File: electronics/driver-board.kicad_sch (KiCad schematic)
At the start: 67 parts, among them J1 Conn_01x02, J3 Motor_Conn_01x04, J5 Conn_01x06_Female, SW1 SW_Push, SW2 SW_Push, U2 LMR16020PDDAR, U3 ESP32-C6-MINI-1/U, U4 AMS1117-3.3, U5 TMC5240-TSSOP38, U6 MT6835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

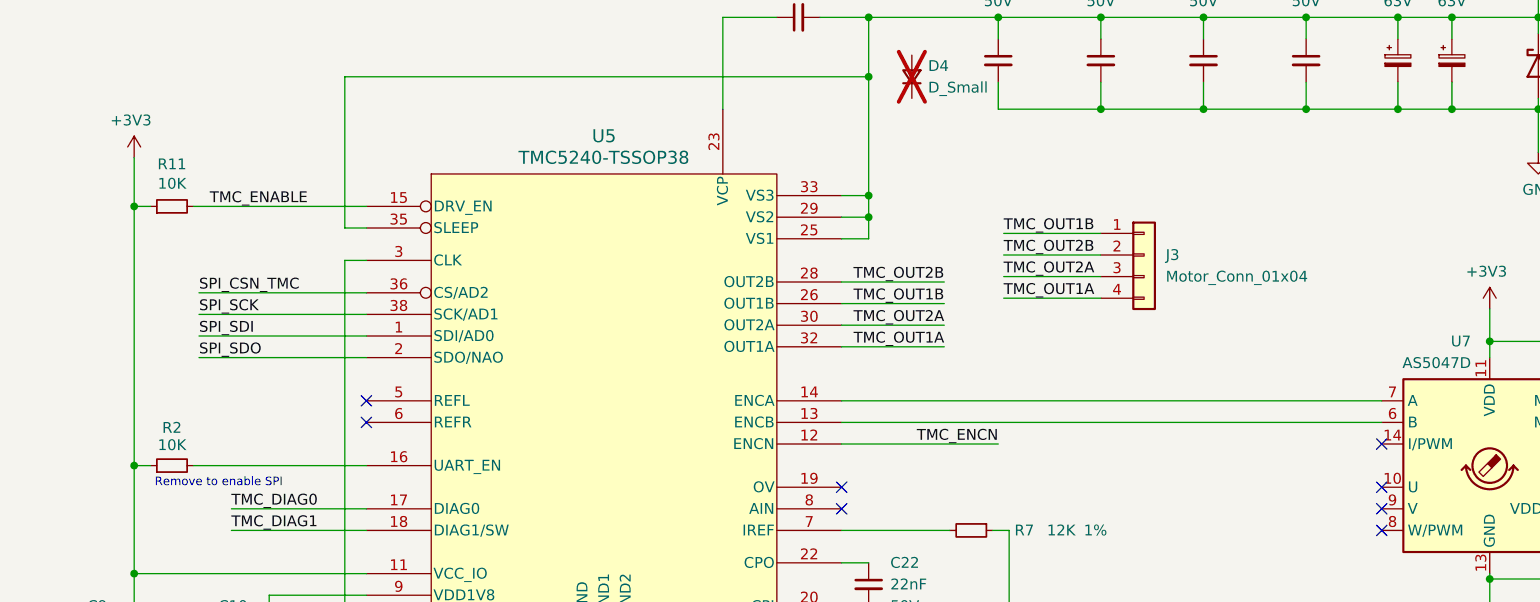
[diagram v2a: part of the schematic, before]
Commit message: connected encoder index
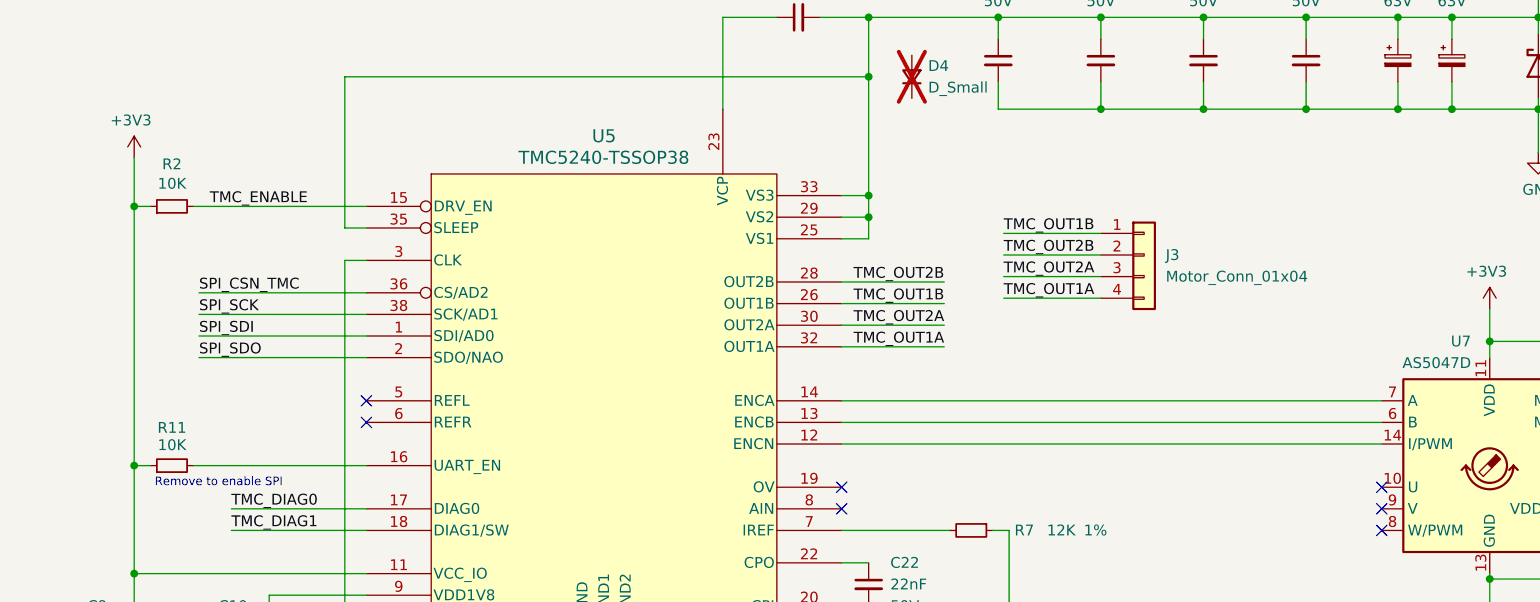
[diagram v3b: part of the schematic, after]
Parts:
- renumbered R2 to R11, R11 to R2
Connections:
- net TMC_ENCN is gone; now on an unnamed net: U5.12 (ENCN)
- no-connect marks 16 -> 15
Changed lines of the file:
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@@
   (no_connect (at 182.88 161.925))
   (no_connect (at 361.315 201.295))
-  (no_connect (at 182.88 156.845))
   (no_connect (at 335.915 196.85))
   (no_connect (at 335.915 191.77))
@@
     (stroke (width 0) (type default))
   )
-  (wire (pts (xy 119.38 156.845) (xy 137.795 156.845))
-    (stroke (width 0) (type default))
-  )
   (wire (pts (xy 96.52 57.785) (xy 96.52 60.325))
     (stroke (width 0) (type default))
@@
     (stroke (width 0) (type default))
   )
+  (wire (pts (xy 119.38 156.845) (xy 182.88 156.845))
+    (stroke (width 0) (type default))
+  )
   (wire (pts (xy 195.58 172.72) (xy 195.58 172.085))
     (stroke (width 0) (type default))
@@
     (effects (font (size 1 1)) (justify right bottom))
   )
-  (label "TMC_ENCN" (at 137.795 156.845 180) (fields_autoplaced)
-    (effects (font (size 1.27 1.27)) (justify right bottom))
-  )
   (label "ESP_UART_RXD" (at 380.365 43.815 180) (fields_autoplaced)
     (effects (font (size 1.27 1.27)) (justify right bottom))
@@
   (symbol (lib_id "Device:R_Small") (at 40.64 159.385 90) (unit 1)
     (in_bom yes) (on_board yes) (dnp no)
-    (property "Reference" "R2" (at 40.64 154.94 90)
+    (property "Reference" "R11" (at 40.64 154.94 90)
       (effects (font (size 1.27 1.27)))
     )
@@
       (project "driver-board"
         (path "/597a11f2-5d2c-4a65-ac95-38ad106e1367"
-          (reference "R2") (unit 1)
+          (reference "R11") (unit 1)
         )
       )
@@
   (symbol (lib_id "Device:R_Small") (at 40.64 128.905 90) (unit 1)
     (in_bom yes) (on_board yes) (dnp no)
-    (property "Reference" "R11" (at 40.64 123.952 90)
+    (property "Reference" "R2" (at 40.64 123.952 90)
       (effects (font (size 1.27 1.27)))
     )
@@
       (project "driver-board"
         (path "/597a11f2-5d2c-4a65-ac95-38ad106e1367"
-          (reference "R11") (unit 1)
+          (reference "R2") (unit 1)
         )
       )

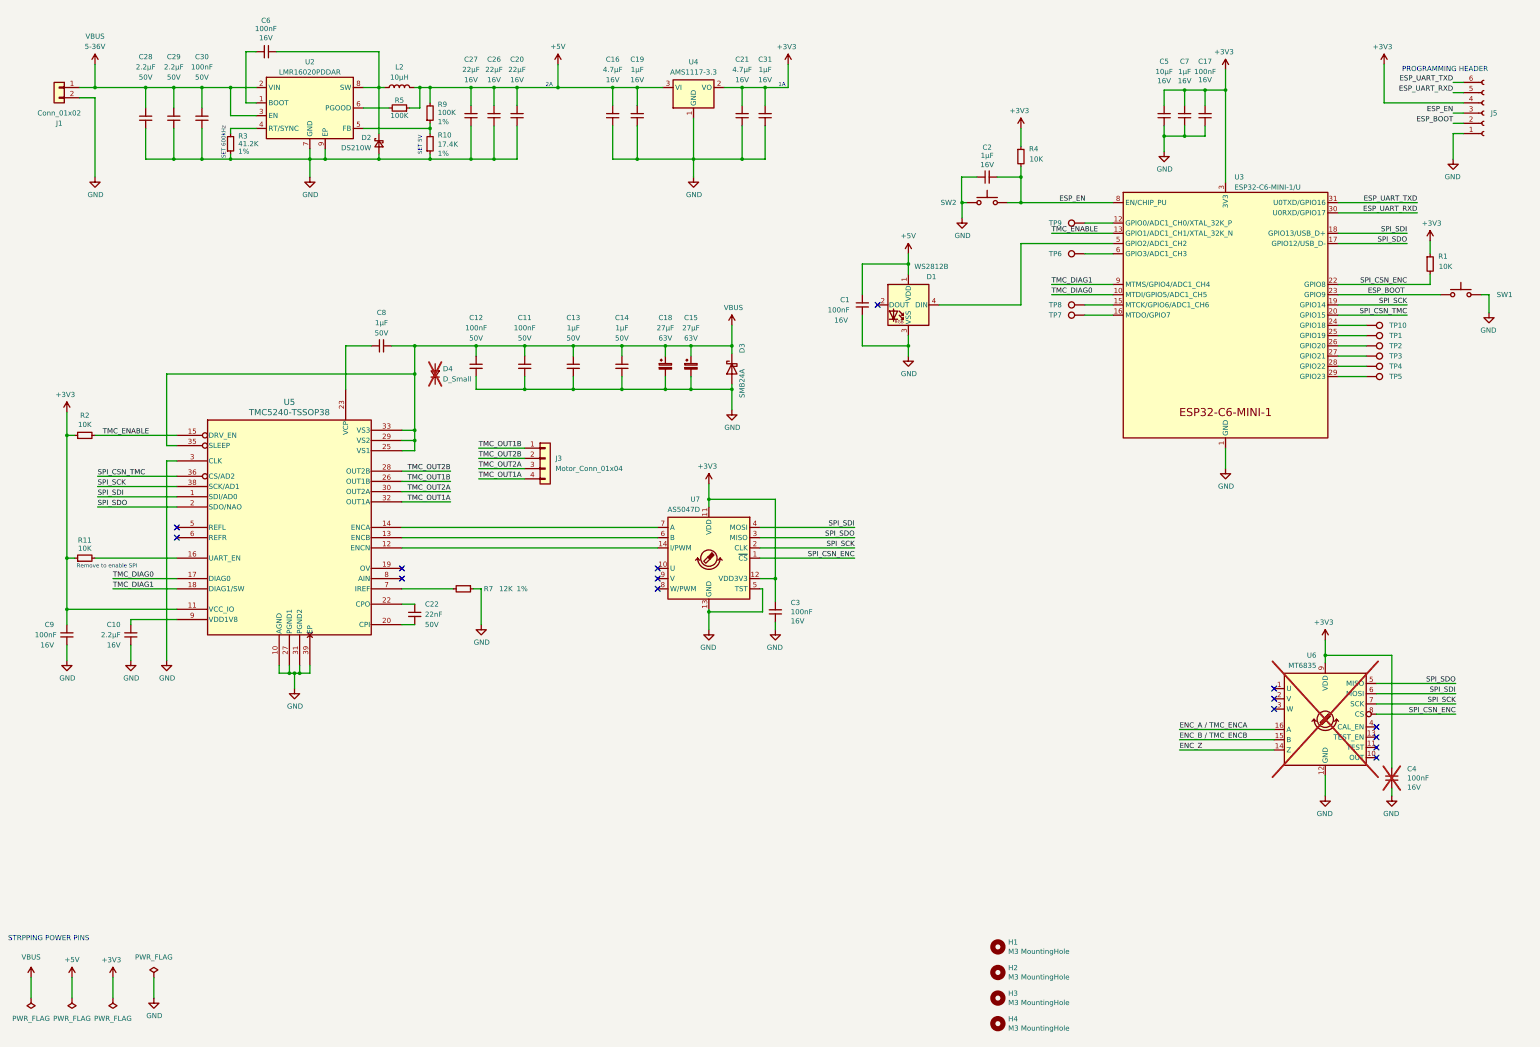
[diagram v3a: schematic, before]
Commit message: new board layout; stripped 5v line and added qwiic and some buttons
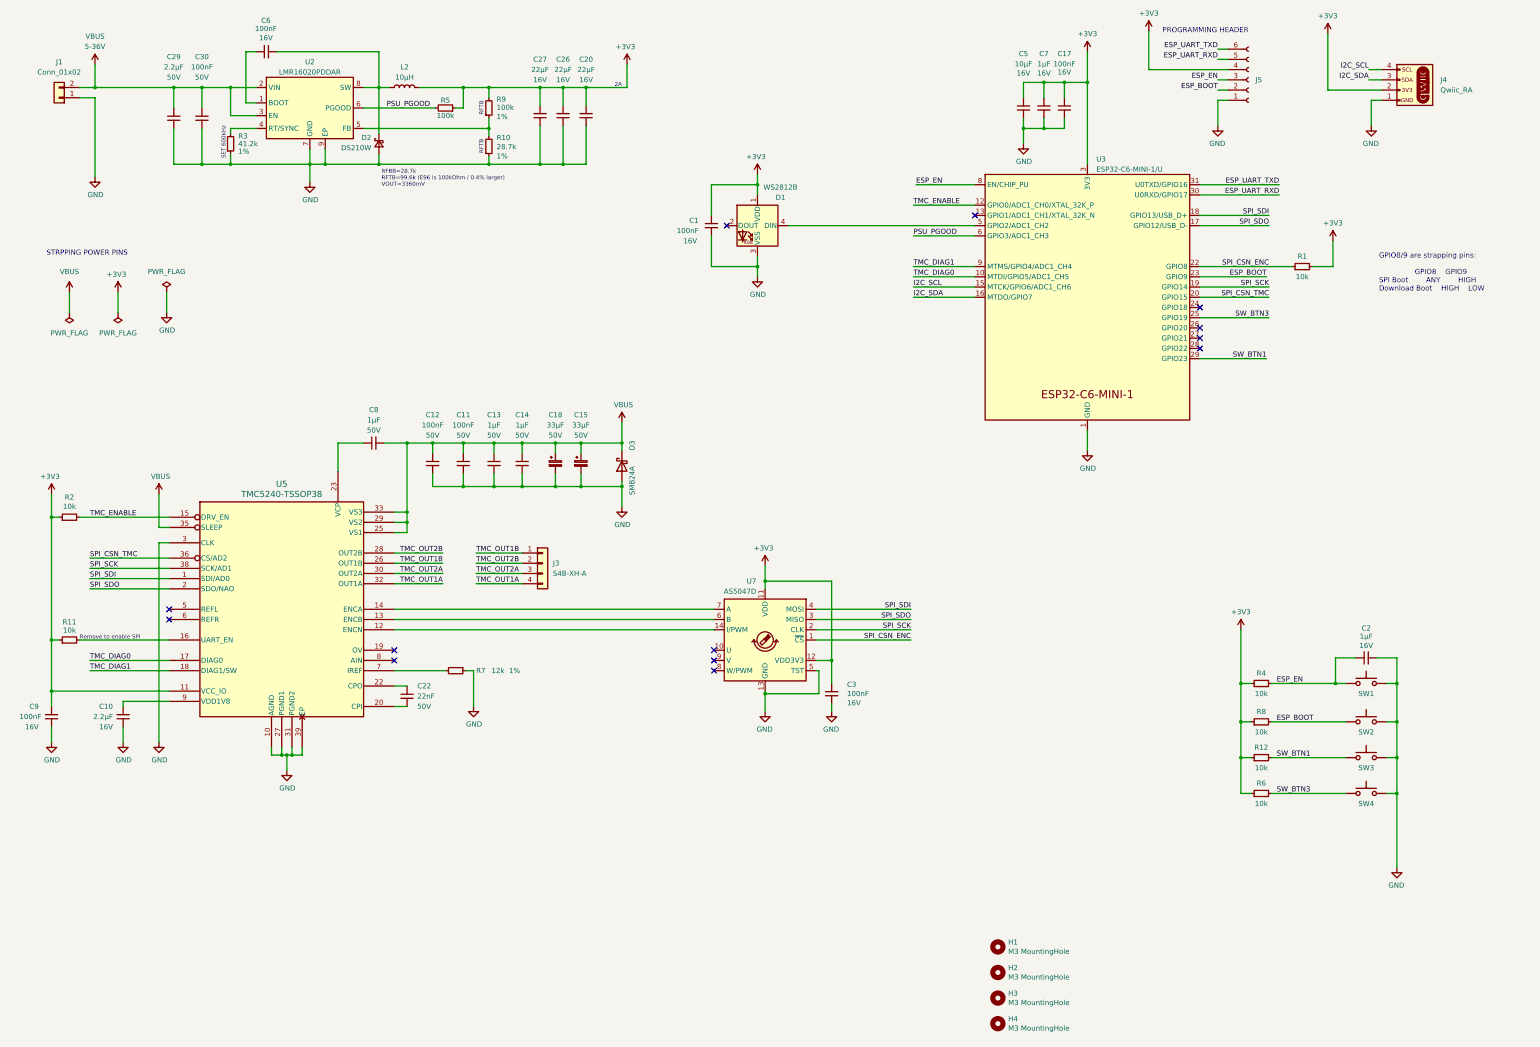
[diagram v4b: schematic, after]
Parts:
- removed C16, C21: 4.7µF, Capacitor_SMD:C_0603_1608Metric, symbol Device:C_Small
- removed C19, C31: 1µF, Capacitor_SMD:C_0603_1608Metric, symbol Device:C_Small
- removed C28: 2.2µF, Capacitor_SMD:C_0603_1608Metric, symbol Device:C_Small
- removed C4: 100nF, Capacitor_SMD:C_0603_1608Metric, symbol Device:C_Small
- removed D4: D_Small, symbol Device:D_Small
- removed TP1, TP10, TP2, TP3, TP4, TP5, TP6, TP7, TP8, TP9: TestPoint, TestPoint:TestPoint_Pad_D1.0mm, symbol Connector:TestPoint
- removed U4: AMS1117-3.3, Package_TO_SOT_SMD:SOT-223-3_TabPin2, symbol Regulator_Linear:AMS1117-3.3
- removed U6: MT6835, Package_SO:TSSOP-16_4.4x5mm_P0.65mm, symbol Slimc_Sensor_Magnetic:MT6835
- added J4: Qwiic_RA, SparkFun-Connector:JST04_1MM_RA, symbol SparkFun-Connector:Qwiic_Right_Angle
- added R12, R6, R8: 10k, Resistor_SMD:R_0603_1608Metric, symbol Device:R_Small
- added SW2, SW4: SW_Push, Slimc_Button_Switch_SMD:SW_Push_1P1T_TS-1145-X-B, symbol Switch:SW_Push
- C15, C18: value 27µF -> 33µF; LCSC C487378 -> C487356; Manf# VKMB1001J270MV -> VKMB1001H330MV; Voltage 63V -> 50V
- J1: footprint Slimc_Connector_Wago:2060-472&slash_998-404 -> Connector_JST:JST_XH_B2B-XH-A_1x02_P2.50mm_Vertical
- J3: value Motor_Conn_01x04 -> S4B-XH-A
- R1, R11, R2, R4: value 10K -> 10k
- R10: value 17.4K -> 28.7k; LCSC C863611 -> C245945; Manf# RT0603FRE0717K4L -> RC0603FR-0728K7L
- R3: value 41.2K -> 41.2k
- R5, R9: value 100K -> 100k
- R7: value 12K -> 12k
- SW3: renamed from SW1; footprint Button_Switch_SMD:SW_SPST_B3U-1000P -> Slimc_Button_Switch_SMD:SW_Push_1P1T_TS-1145-X-B; LCSC C231329 -> C5146819; Manf Omron Electronics -> XKB Connectivity; Manf# B3U-1000P -> TS-1145-B-B
- renumbered SW2 to SW1
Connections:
- net +5V is gone; now on net +3V3: C1.1, C20.2, C26.2, C27.2, D1.1 (VDD), L2.2, R5.1, R9.2
- net +3V3: now also R1.2, J4.2 (Pin_2), R12.1, R6.1, R8.1; no longer R1.1
- net ESP_BOOT: now also R8.2, SW2.2; no longer SW3.2
- net ESP_EN: now also C2.1, SW1.1; no longer C2.2, SW1.2
- net GND: now also C2.2, J1.1 (Pin_1), SW1.2, J4.1 (Pin_1), SW2.1, SW4.1; no longer C2.1, J1.2 (Pin_2), SW1.1
- net SPI_CSN_ENC: now also R1.1; no longer R1.2
- net TMC_ENABLE: now also U3.12 (GPIO0/ADC1_CH0/XTAL_32K_P); no longer U3.13 (GPIO1/ADC1_CH1/XTAL_32K_N)
- net VBUS: now also J1.2 (Pin_2); no longer J1.1 (Pin_1)
- net PSU_PGOOD: now reaches R5.2, U2.6 (PGOOD)
- net PSU_PGOOD: now also U3.6 (GPIO3/ADC1_CH3)
- net SW_BTN1: now reaches U3.29 (GPIO23)
- net SW_BTN1: now also SW3.2, R12.2
- net SW_BTN3: now reaches U3.25 (GPIO19)
- net SW_BTN3: now also R6.2, SW4.2
- net I2C_SCL: now reaches U3.15 (MTCK/GPIO6/ADC1_CH6)
- net I2C_SCL: now also J4.4 (Pin_4)
- net I2C_SDA: now reaches U3.16 (MTDO/GPIO7)
- net I2C_SDA: now also J4.3 (Pin_3)
- new net: J4.NC1 (NC), J4.NC2 (NC)
- no-connect marks 15 -> 13
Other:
- note added: "GPIO8/9 are strapping pins: GPIO8 GPIO9 SPI Boot ANY HIGH Download Boot HIGH LOW"
- note added: "RFBB=28.7k RFTB=99.6k (E96 is 100kOhm / 0.4% larger) VOUT=3360mV"
- note added: "RFTB"
- note removed: "1A"
- note removed: "SET 5V"
- moved on the sheet: C1, C10, C11, C12, C13, C14, C17, C18, C2, C20, C22, C26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

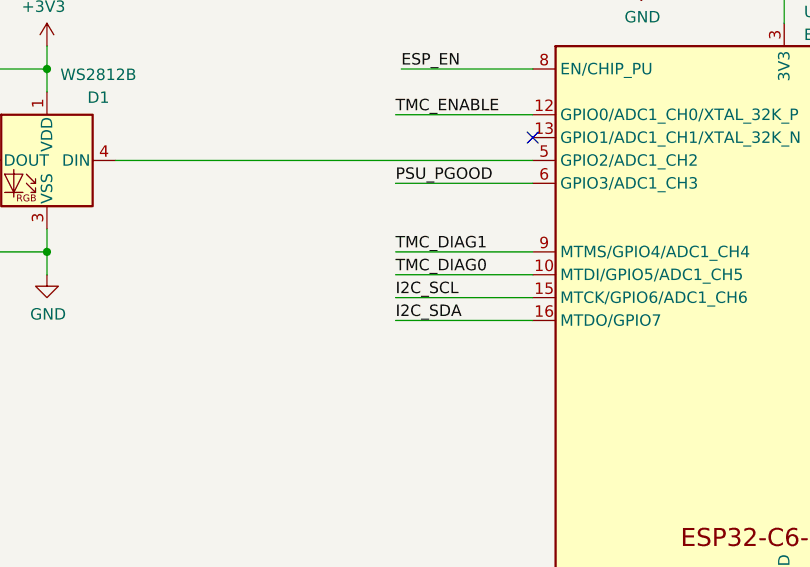
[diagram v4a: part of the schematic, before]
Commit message: pull ups for i2c; teardrops on through hole connections
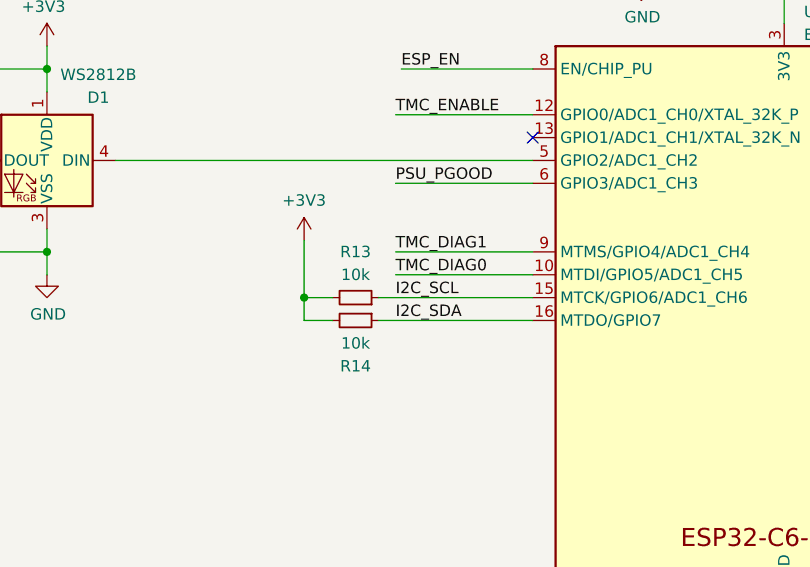
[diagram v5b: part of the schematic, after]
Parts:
- added R13, R14: 10k, Resistor_SMD:R_0603_1608Metric, symbol Device:R_Small
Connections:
- net +3V3: now also R13.2, R14.2
- net I2C_SCL: now also R13.1
- net I2C_SDA: now also R14.1
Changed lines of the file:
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@@
   (junction (at 289.56 41.275) (diameter 0) (color 0 0 0 0)
   )
+  (junction (at 236.22 92.075) (diameter 0) (color 0 0 0 0)
+  )
   (junction (at 120.65 147.955) (diameter 0) (color 0 0 0 0)
   )
@@
     (stroke (width 0) (type default))
   )
-  (wire (pts (xy 261.62 94.615) (xy 246.38 94.615))
+  (wire (pts (xy 261.62 94.615) (xy 244.475 94.615))
     (stroke (width 0) (type default))
   )
@@
     (stroke (width 0) (type default))
   )
+  (wire (pts (xy 236.22 94.615) (xy 236.22 92.075))
+    (stroke (width 0) (type default))
+  )
   (wire (pts (xy 222.885 187.325) (xy 222.885 193.04))
     (stroke (width 0) (type default))
@@
     (stroke (width 0) (type default))
   )
+  (wire (pts (xy 236.22 85.725) (xy 236.22 92.075))
+    (stroke (width 0) (type default))
+  )
   (wire (pts (xy 351.155 190.5) (xy 353.695 190.5))
     (stroke (width 0) (type default))
@@
     (stroke (width 0) (type default))
   )
-  (wire (pts (xy 261.62 92.075) (xy 246.38 92.075))
+  (wire (pts (xy 261.62 92.075) (xy 244.475 92.075))
     (stroke (width 0) (type default))
   )
@@
     (stroke (width 0) (type default))
   )
+  (wire (pts (xy 239.395 92.075) (xy 236.22 92.075))
+    (stroke (width 0) (type default))
+  )
   (wire (pts (xy 278.765 45.085) (xy 278.765 41.275))
     (stroke (width 0) (type default))
@@
     (stroke (width 0) (type default))
   )
+  (wire (pts (xy 239.395 94.615) (xy 236.22 94.615))
+    (stroke (width 0) (type default))
+  )
   (wire (pts (xy 245.745 172.085) (xy 222.25 172.085))
     (stroke (width 0) (type default))
@@
     )
   )
+  (symbol (lib_id "Device:R_Small") (at 241.935 94.615 270) (unit 1)
+    (in_bom yes) (on_board yes) (dnp no)
+    (property "Reference" "R14" (at 241.935 99.695 90)
+      (effects (font (size 1.27 1.27)))
+    )
+    (property "Value" "10k" (at 241.935 97.155 90)
+      (effects (font (size 1.27 1.27)))
+    )
+    (property "Footprint" "Resistor_SMD:R_0603_1608Metric" (at 241.935 94.615 0)
+      (effects (font (size 1.27 1.27)) hide)
+    )
+    (property "Datasheet" "~" (at 241.935 94.615 0)
+      (effects (font (size 1.27 1.27)) hide)
+    )
+    (property "Manf#" "RT0603FRE1310KL" (at 241.935 94.615 0)
+      (effects (font (size 1.27 1.27)) hide)
+    )
+    (property "LCSC" "C4226066" (at 241.935 94.615 0)
+      (effects (font (size 1.27 1.27)) hide)
+    )
+    (property "Package" "0603" (at 241.935 94.615 0)
+      (effects (font (size 1.27 1.27)) hide)
+    )
+    (pin "1")
+    (pin "2")
+    (instances
+      (project "driver-board"
+        (path "/597a11f2-5d2c-4a65-ac95-38ad106e1367"
+          (reference "R14") (unit 1)
+        )
+      )
+    )
+  )
   (symbol (lib_id "Device:C_Small") (at 50.165 198.755 180) (unit 1)
     (in_bom yes) (on_board yes) (dnp no)
@@
     )
   )
+  (symbol (lib_id "Device:R_Small") (at 241.935 92.075 270) (mirror x) (unit 1)
+    (in_bom yes) (on_board yes) (dnp no)
+    (property "Reference" "R13" (at 241.935 86.995 90)
+      (effects (font (size 1.27 1.27)))
+    )
+    (property "Value" "10k" (at 241.935 89.535 90)
+      (effects (font (size 1.27 1.27)))
+    )
+    (property "Footprint" "Resistor_SMD:R_0603_1608Metric" (at 241.935 92.075 0)
+      (effects (font (size 1.27 1.27)) hide)
+    )
+    (property "Datasheet" "~" (at 241.935 92.075 0)
+      (effects (font (size 1.27 1.27)) hide)
+    )
+    (property "Manf#" "RT0603FRE1310KL" (at 241.935 92.075 0)
+      (effects (font (size 1.27 1.27)) hide)
+    )
+    (property "LCSC" "C4226066" (at 241.935 92.075 0)
+      (effects (font (size 1.27 1.27)) hide)
+    )
+    (property "Package" "0603" (at 241.935 92.075 0)
+      (effects (font (size 1.27 1.27)) hide)
+    )
+    (pin "1")
+    (pin "2")
+    (instances
+      (project "driver-board"
+        (path "/597a11f2-5d2c-4a65-ac95-38ad106e1367"
+          (reference "R13") (unit 1)
+        )
+      )
+    )
+  )
   (symbol (lib_id "Device:R_Small") (at 36.83 149.225 90) (unit 1)
     (in_bom yes) (on_board yes) (dnp no)
@@
         )
       )
+    )
+  )
+  (symbol (lib_id "power:+3V3") (at 236.22 85.725 0) (mirror y) (unit 1)
+    (in_bom yes) (on_board yes) (dnp no)
+    (property "Reference" "#PWR016" (at 236.22 89.535 0)
+      (effects (font (size 1.27 1.27)) hide)
+    )
+    (property "Value" "+3V3" (at 236.22 81.28 0)
+      (effects (font (size 1.27 1.27)))
+    )
+    (property "Footprint" "" (at 236.22 85.725 0)
+      (effects (font (size 1.27 1.27)) hide)
+    )
+    (property "Datasheet" "" (at 236.22 85.725 0)
+      (effects (font (size 1.27 1.27)) hide)
+    )
+    (pin "1")
+    (instances
+      (project "driver-board"
+        (path "/597a11f2-5d2c-4a65-ac95-38ad106e1367"
+          (reference "#PWR016") (unit 1)
+        )
+      )
